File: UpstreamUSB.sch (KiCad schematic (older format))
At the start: 4 parts

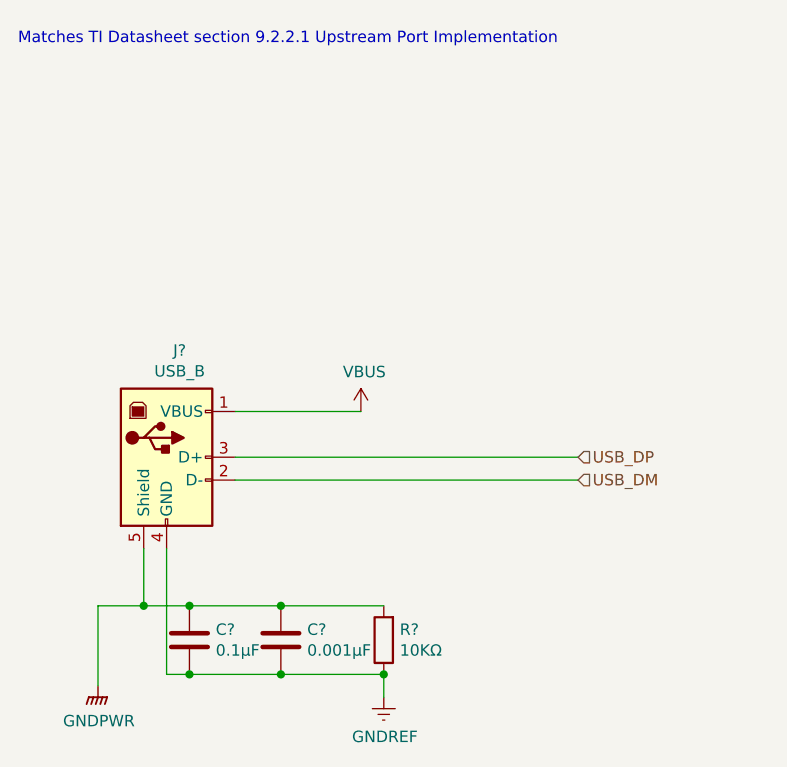
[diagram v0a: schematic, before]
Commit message: Moved clock to its own page
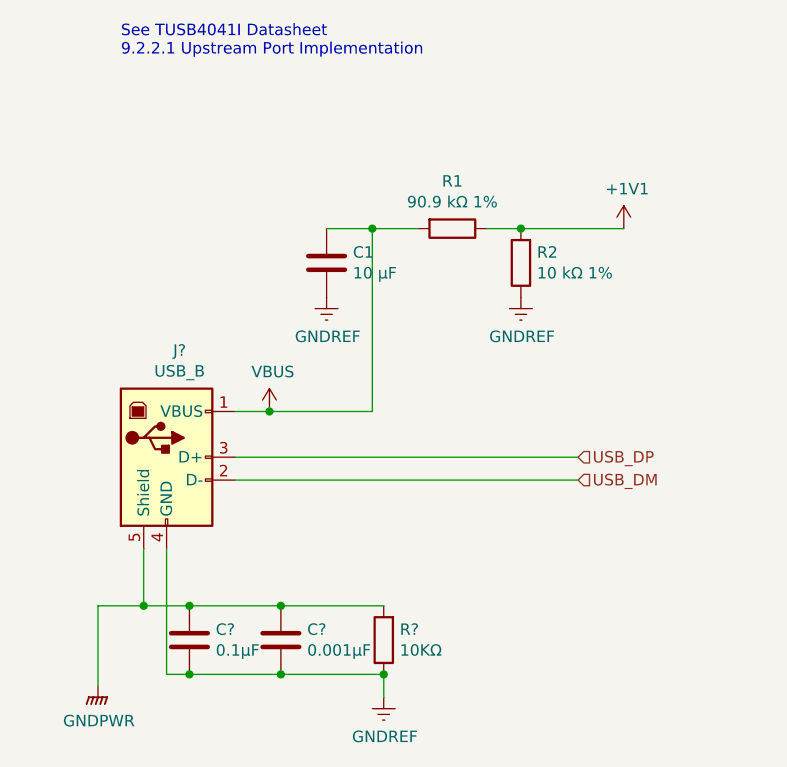
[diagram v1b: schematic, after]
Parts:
- added C1: 10 μF, symbol Device:C
- added R1: 90.9 kΩ 1%, symbol Device:R
- added R2: 10 kΩ 1%, symbol Device:R
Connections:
- net GNDREF: now also C1.2, R2.1
- net VBUS: now also C1.1, R1.2
- new net +1V1: R1.1, R2.2
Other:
- note added: "See TUSB4041I Datasheet\n9.2.2.1 Upstream Port Implementation"
- note removed: "Matches TI Datasheet section 9.2.2.1 Upstream Port Implementation"
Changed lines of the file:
@@
 $Descr A4 11693 8268
 encoding utf-8
-Sheet 2 5
+Sheet 2 6
 Title ""
 Date ""
@@
 	1    0    0    -1
 $EndComp
-Wire Wire Line
-	4800 2950 5350 2950
 $Comp
 L Connector:USB_B J?
@@
 	1    0    0    -1
 $EndComp
-Text Notes 3850 1350 0    50   ~ 0
-Matches TI Datasheet section 9.2.2.1 Upstream Port Implementation
+Text Notes 4300 1400 0    50   ~ 0
+See TUSB4041I Datasheet\n9.2.2.1 Upstream Port Implementation
+$Comp
+L Device:C C?
+U 1 1 604E15AE
+P 5200 2300
+AR Path="/604E15AE" Ref="C?"  Part="1"
+AR Path="/6057976E/604E15AE" Ref="C1"  Part="1"
+F 0 "C1" H 5315 2346 50  0000 L CNN
+F 1 "10 μF" H 5315 2255 50  0000 L CNN
+F 2 "" H 5238 2150 50  0001 C CNN
+F 3 "~" H 5200 2300 50  0001 C CNN
+	1    5200 2300
+	1    0    0    -1
+$EndComp
+Connection ~ 6050 2150
+Wire Wire Line
+	6050 2150 6500 2150
+Wire Wire Line
+	5900 2150 6050 2150
+$Comp
+L Device:R R?
+U 1 1 604E15B7
+P 6050 2300
+AR Path="/604E15B7" Ref="R?"  Part="1"
+AR Path="/6057976E/604E15B7" Ref="R2"  Part="1"
+F 0 "R2" H 5980 2254 50  0000 R CNN
+F 1 "10 kΩ 1%" H 5980 2345 50  0000 R CNN
+F 2 "" V 5980 2300 50  0001 C CNN
+F 3 "~" H 6050 2300 50  0001 C CNN
+	1    6050 2300
+	-1   0    0    1
+$EndComp
+$Comp
+L Device:R R?
+U 1 1 604E15BD
+P 5750 2150
+AR Path="/604E15BD" Ref="R?"  Part="1"
+AR Path="/6057976E/604E15BD" Ref="R1"  Part="1"
+F 0 "R1" V 5543 2150 50  0000 C CNN
+F 1 "90.9 kΩ 1%" V 5634 2150 50  0000 C CNN
+F 2 "" V 5680 2150 50  0001 C CNN
+F 3 "~" H 5750 2150 50  0001 C CNN
+	1    5750 2150
+	0    1    1    0
+$EndComp
+$Comp
+L power:GNDREF #PWR?
+U 1 1 604E15C3
+P 6050 2450
+AR Path="/6057976E/604E15C3" Ref="#PWR?"  Part="1"
+AR Path="/604E15C3" Ref="#PWR?"  Part="1"
+F 0 "#PWR?" H 6050 2200 50  0001 C CNN
+F 1 "GNDREF" H 6055 2277 50  0000 C CNN
+F 2 "" H 6050 2450 50  0001 C CNN
+F 3 "" H 6050 2450 50  0001 C CNN
+	1    6050 2450
+	1    0    0    -1
+$EndComp
+$Comp
+L power:GNDREF #PWR?
+U 1 1 604E15C9
+P 5200 2450
+AR Path="/6057976E/604E15C9" Ref="#PWR?"  Part="1"
+AR Path="/604E15C9" Ref="#PWR?"  Part="1"
+F 0 "#PWR?" H 5200 2200 50  0001 C CNN
+F 1 "GNDREF" H 5205 2277 50  0000 C CNN
+F 2 "" H 5200 2450 50  0001 C CNN
+F 3 "" H 5200 2450 50  0001 C CNN
+	1    5200 2450
+	1    0    0    -1
+$EndComp
+Wire Wire Line
+	5200 2150 5400 2150
 $Comp
 L power:VBUS #PWR?
-U 1 1 605D5455
-P 5350 2950
-F 0 "#PWR?" H 5350 2800 50  0001 C CNN
-F 1 "VBUS" H 5365 3123 50  0000 C CNN
-F 2 "" H 5350 2950 50  0001 C CNN
-F 3 "" H 5350 2950 50  0001 C CNN
-	1    5350 2950
-	1    0    0    -1
-$EndComp
+U 1 1 604E15D0
+P 4950 2950
+AR Path="/604E15D0" Ref="#PWR?"  Part="1"
+AR Path="/6057976E/604E15D0" Ref="#PWR?"  Part="1"
+F 0 "#PWR?" H 4950 2800 50  0001 C CNN
+F 1 "VBUS" H 4965 3123 50  0000 C CNN
+F 2 "" H 4950 2950 50  0001 C CNN
+F 3 "" H 4950 2950 50  0001 C CNN
+	1    4950 2950
+	1    0    0    -1
+$EndComp
+Connection ~ 5400 2150
+Wire Wire Line
+	5400 2150 5600 2150
+Wire Wire Line
+	5400 2150 5400 2950
+Wire Wire Line
+	4800 2950 4950 2950
+Connection ~ 4950 2950
+Wire Wire Line
+	4950 2950 5400 2950
+$Comp
+L power:+1V1 #PWR?
+U 1 1 604E6D5F
+P 6500 2150
+F 0 "#PWR?" H 6500 2000 50  0001 C CNN
+F 1 "+1V1" H 6515 2323 50  0000 C CNN
+F 2 "" H 6500 2150 50  0001 C CNN
+F 3 "" H 6500 2150 50  0001 C CNN
+	1    6500 2150
+	1    0    0    -1
+$EndComp

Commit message: First pass at pcb layout
Not really ready to set that in stone, but wanted to get an idea of what size enclosure will work.
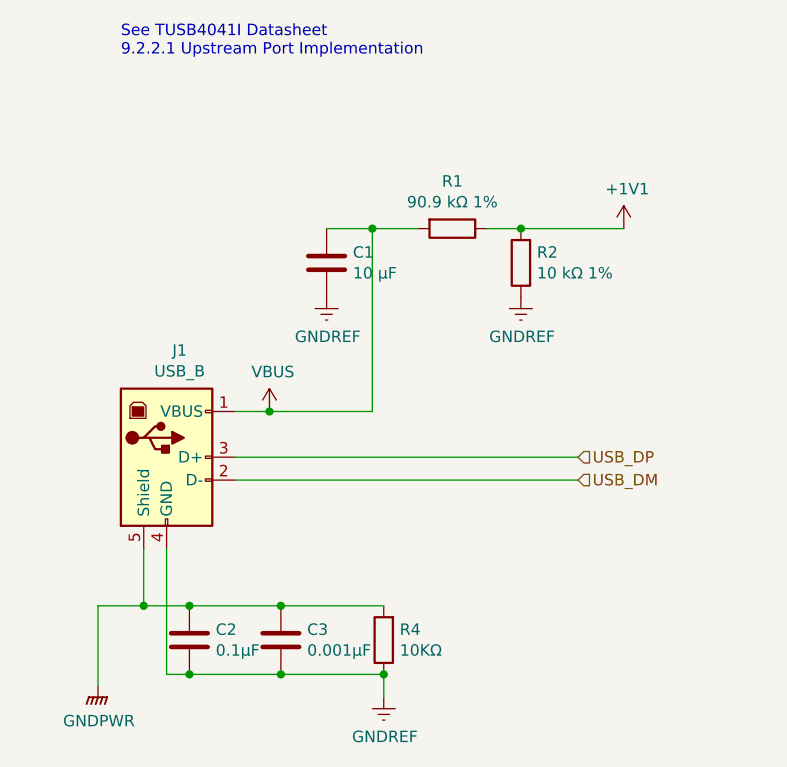
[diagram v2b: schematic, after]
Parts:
- C1: footprint (none) -> Capacitor_SMD:C_1210_3225Metric
- C2, C3: renamed from C?; footprint (none) -> Capacitor_SMD:C_1210_3225Metric
- J1: renamed from J?; footprint (none) -> Connector_USB:USB_Mini-B_Lumberg_2486_01_Horizontal
- R1, R2: footprint (none) -> Resistor_SMD:R_1210_3225Metric
- R4: renamed from R?; footprint (none) -> Resistor_SMD:R_1210_3225Metric
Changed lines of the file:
@@
 P 5450 3950
 AR Path="/605700C9" Ref="R?"  Part="1"
-AR Path="/6057976E/605700C9" Ref="R?"  Part="1"
-F 0 "R?" H 5380 3904 50  0000 R CNN
+AR Path="/6057976E/605700C9" Ref="R4"  Part="1"
+F 0 "R4" H 5380 3904 50  0000 R CNN
 F 1 "10KΩ" H 5380 3995 50  0000 R CNN
-F 2 "" V 5380 3950 50  0001 C CNN
+F 2 "Resistor_SMD:R_1210_3225Metric" V 5380 3950 50  0001 C CNN
 F 3 "~" H 5450 3950 50  0001 C CNN
 	1    5450 3950
@@
 P 5000 3950
 AR Path="/605700CF" Ref="C?"  Part="1"
-AR Path="/6057976E/605700CF" Ref="C?"  Part="1"
-F 0 "C?" H 5115 3996 50  0000 L CNN
+AR Path="/6057976E/605700CF" Ref="C3"  Part="1"
+F 0 "C3" H 5115 3996 50  0000 L CNN
 F 1 "0.001μF" H 5115 3905 50  0000 L CNN
-F 2 "" H 5038 3800 50  0001 C CNN
+F 2 "Capacitor_SMD:C_1210_3225Metric" H 5038 3800 50  0001 C CNN
 F 3 "~" H 5000 3950 50  0001 C CNN
 	1    5000 3950
@@
 P 4600 3950
 AR Path="/605700D5" Ref="C?"  Part="1"
-AR Path="/6057976E/605700D5" Ref="C?"  Part="1"
-F 0 "C?" H 4715 3996 50  0000 L CNN
+AR Path="/6057976E/605700D5" Ref="C2"  Part="1"
+F 0 "C2" H 4715 3996 50  0000 L CNN
 F 1 "0.1μF" H 4715 3905 50  0000 L CNN
-F 2 "" H 4638 3800 50  0001 C CNN
+F 2 "Capacitor_SMD:C_1210_3225Metric" H 4638 3800 50  0001 C CNN
 F 3 "~" H 4600 3950 50  0001 C CNN
 	1    4600 3950
@@
 P 4500 3150
 AR Path="/60570101" Ref="J?"  Part="1"
-AR Path="/6057976E/60570101" Ref="J?"  Part="1"
-F 0 "J?" H 4557 3617 50  0000 C CNN
+AR Path="/6057976E/60570101" Ref="J1"  Part="1"
+F 0 "J1" H 4557 3617 50  0000 C CNN
 F 1 "USB_B" H 4557 3526 50  0000 C CNN
-F 2 "" H 4650 3100 50  0001 C CNN
+F 2 "Connector_USB:USB_Mini-B_Lumberg_2486_01_Horizontal" H 4650 3100 50  0001 C CNN
 F 3 " ~" H 4650 3100 50  0001 C CNN
 	1    4500 3150
@@
 	4800 3250 6300 3250
 $Comp
-L power:GNDPWR #PWR?
+L power:GNDPWR #PWR0104
 U 1 1 6058B2D9
 P 4200 4150
-F 0 "#PWR?" H 4200 3950 50  0001 C CNN
+F 0 "#PWR0104" H 4200 3950 50  0001 C CNN
 F 1 "GNDPWR" H 4204 3996 50  0000 C CNN
 F 2 "" H 4200 4100 50  0001 C CNN
@@
 	4200 3800 4200 4150
 $Comp
-L power:GNDREF #PWR?
+L power:GNDREF #PWR0105
 U 1 1 6058D96C
 P 5450 4200
-F 0 "#PWR?" H 5450 3950 50  0001 C CNN
+F 0 "#PWR0105" H 5450 3950 50  0001 C CNN
 F 1 "GNDREF" H 5455 4027 50  0000 C CNN
 F 2 "" H 5450 4200 50  0001 C CNN
@@
 F 0 "C1" H 5315 2346 50  0000 L CNN
 F 1 "10 μF" H 5315 2255 50  0000 L CNN
-F 2 "" H 5238 2150 50  0001 C CNN
+F 2 "Capacitor_SMD:C_1210_3225Metric" H 5238 2150 50  0001 C CNN
 F 3 "~" H 5200 2300 50  0001 C CNN
 	1    5200 2300
@@
 F 0 "R2" H 5980 2254 50  0000 R CNN
 F 1 "10 kΩ 1%" H 5980 2345 50  0000 R CNN
-F 2 "" V 5980 2300 50  0001 C CNN
+F 2 "Resistor_SMD:R_1210_3225Metric" V 5980 2300 50  0001 C CNN
 F 3 "~" H 6050 2300 50  0001 C CNN
 	1    6050 2300
@@
 F 0 "R1" V 5543 2150 50  0000 C CNN
 F 1 "90.9 kΩ 1%" V 5634 2150 50  0000 C CNN
-F 2 "" V 5680 2150 50  0001 C CNN
+F 2 "Resistor_SMD:R_1210_3225Metric" V 5680 2150 50  0001 C CNN
 F 3 "~" H 5750 2150 50  0001 C CNN
 	1    5750 2150
@@
 $EndComp
 $Comp
-L power:GNDREF #PWR?
+L power:GNDREF #PWR0106
 U 1 1 604E15C3
 P 6050 2450
-AR Path="/6057976E/604E15C3" Ref="#PWR?"  Part="1"
+AR Path="/6057976E/604E15C3" Ref="#PWR0106"  Part="1"
 AR Path="/604E15C3" Ref="#PWR?"  Part="1"
-F 0 "#PWR?" H 6050 2200 50  0001 C CNN
+F 0 "#PWR0106" H 6050 2200 50  0001 C CNN
 F 1 "GNDREF" H 6055 2277 50  0000 C CNN
 F 2 "" H 6050 2450 50  0001 C CNN
@@
 $EndComp
 $Comp
-L power:GNDREF #PWR?
+L power:GNDREF #PWR0107
 U 1 1 604E15C9
 P 5200 2450
-AR Path="/6057976E/604E15C9" Ref="#PWR?"  Part="1"
+AR Path="/6057976E/604E15C9" Ref="#PWR0107"  Part="1"
 AR Path="/604E15C9" Ref="#PWR?"  Part="1"
-F 0 "#PWR?" H 5200 2200 50  0001 C CNN
+F 0 "#PWR0107" H 5200 2200 50  0001 C CNN
 F 1 "GNDREF" H 5205 2277 50  0000 C CNN
 F 2 "" H 5200 2450 50  0001 C CNN
@@
 P 4950 2950
 AR Path="/604E15D0" Ref="#PWR?"  Part="1"
-AR Path="/6057976E/604E15D0" Ref="#PWR?"  Part="1"
-F 0 "#PWR?" H 4950 2800 50  0001 C CNN
+AR Path="/6057976E/604E15D0" Ref="#PWR0108"  Part="1"
+F 0 "#PWR0108" H 4950 2800 50  0001 C CNN
 F 1 "VBUS" H 4965 3123 50  0000 C CNN
 F 2 "" H 4950 2950 50  0001 C CNN
@@
 	4950 2950 5400 2950
 $Comp
-L power:+1V1 #PWR?
+L power:+1V1 #PWR0109
 U 1 1 604E6D5F
 P 6500 2150
-F 0 "#PWR?" H 6500 2000 50  0001 C CNN
+F 0 "#PWR0109" H 6500 2000 50  0001 C CNN
 F 1 "+1V1" H 6515 2323 50  0000 C CNN
 F 2 "" H 6500 2150 50  0001 C CNN

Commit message: Swap TUSB4041I for TUSB2036
The 4041 does more than I need it to, so use the 2036 instead.
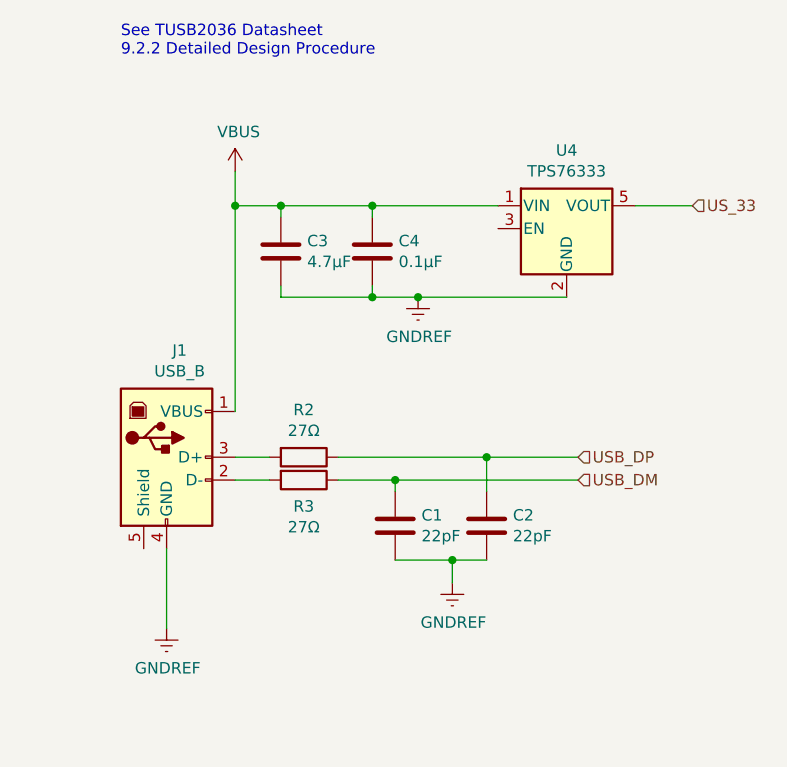
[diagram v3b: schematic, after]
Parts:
- removed R1: 90.9 kΩ 1%, Resistor_SMD:R_1210_3225Metric, symbol Device:R
- removed R4: 10KΩ, Resistor_SMD:R_1210_3225Metric, symbol Device:R
- added C4: 0.1μF, Capacitor_SMD:C_1210_3225Metric, symbol Device:C
- added R3: 27Ω, Resistor_SMD:R_1210_3225Metric, symbol Device:R
- added U4: TPS76333, Package_TO_SOT_SMD:SOT-23-5, symbol Regulator_Linear:TPS76333
- C1: value 10 μF -> 22pF
- C2: value 0.1μF -> 22pF
- C3: value 0.001μF -> 4.7μF
- J1: footprint Connector_USB:USB_Mini-B_Lumberg_2486_01_Horizontal -> Connector_USB:USB_Micro-B_Molex_47346-0001
- R2: value 10 kΩ 1% -> 27Ω
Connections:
- net GNDREF: now also C4.2, U4.2 (GND); no longer R2.1
- net USB_DM: now also C1.1, R3.1; no longer J1.2 (D-)
- net USB_DP: now also C2.1, R2.1; no longer J1.3 (D+)
- net VBUS: now also C3.1, C4.1, U4.1 (VIN); no longer C1.1
- net +1V1: no longer names the net of R2.2
- net +1V1: now also J1.3 (D+)
- removed net GNDPWR: C2.1, C3.1, J1.5 (Shield)
- new net: J1.2 (D-), R3.2
- new net US_33: U4.5 (VOUT)
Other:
- note added: "See TUSB2036 Datasheet\n9.2.2 Detailed Design Procedure"
- note removed: "See TUSB4041I Datasheet\n9.2.2.1 Upstream Port Implementation"
